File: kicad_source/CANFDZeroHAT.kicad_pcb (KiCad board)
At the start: 2 copper layers, 65 x 30 mm, 2 parts, among them CN1 RASPI-IO

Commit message: generated schematic and layout
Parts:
- removed ?: , 
- added C1: 100nF, capacitors:C_0603, F.Cu at (133.5, 96.5)
- added C2: 22pF, capacitors:C_0603, F.Cu at (141.0, 106.0)
- added C3: 22pF, capacitors:C_0603, F.Cu at (141.0, 100.0)
- added C4: 100nF, capacitors:C_0603, F.Cu at (154.5, 97.5)
- added CN2: CONN_01X04, CON_wuerth:WR-TBL_691210910004, F.Cu at (135.5, 113.0)
- added CN3: GH_SM04B-GHS-TB, Connector_JST:JST_GH_SM04B-GHS-TB_1x04-1MP_P1.25mm_Horizontal, F.Cu at (159.5, 113.0)
- added CN4: GH_SM04B-GHS-TB, Connector_JST:JST_GH_SM04B-GHS-TB_1x04-1MP_P1.25mm_Horizontal, F.Cu at (149.0, 113.0)
- added D1: DNI, diodes:SOD-123, F.Cu at (142.5, 108.5)
- added L1: Label, labels:generationmake_small_solder, F.Cu at (164.4, 98.5)
- added L2: Label, labels:generationmake_logo, F.Cu at (119.6, 100.7)
- added R1: 0R, resistors:R_0603, F.Cu at (148.5, 94.5)
- added R2: DNI, resistors:R_0603, F.Cu at (150.5, 94.5)
- added R3: 10k, resistors:R_0603, F.Cu at (152.5, 94.5)
- added R4: 120R, resistors:R_0603, F.Cu at (127.0, 103.5)
- added R5: 10k, resistors:R_0603, F.Cu at (137.0, 94.5)
- added SW1: JS202011JCQN, mechanical-switches:CK_JS202011JCQN, F.Cu at (122.7, 105.5)
- added U1: MCP2517FD, SOIC:SOIC-14_3.9x8.7mm_Pitch1.27mm, F.Cu at (148.0, 101.5)
- added U2: SN65HVD232, SOIC:SOIJ-8_5.3x5.3mm_Pitch1.27mm, F.Cu at (133.5, 102.5)
- added Y1: RH100-20.000-20-3030-TR, crystals:Crystal_SMD_3.2x2.5mm_4Pad, F.Cu at (141.0, 103.0)
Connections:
- CN1 pad 19: (no net) -> /SPI_MOSI
- CN1 pad 21: (no net) -> /SPI_MISO
- CN1 pad 22: (no net) -> /MCP2517_INT
- CN1 pad 23: (no net) -> /SPI_CLK
- CN1 pad 24: (no net) -> /SPI_CE0
- CN1 pad 26: (no net) -> /SPI_CE1
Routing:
- net GND: track 0.00 -> 156.8 mm, vias 0 -> 4
- net +3V3: track 0.00 -> 55.5 mm, vias 0 -> 2
- net /CANH: track 0.00 -> 52.9 mm
- net +5V: track 0.00 -> 48.7 mm
- net /CANL: track 0.00 -> 48.5 mm
- net /MCP2517_INT: track 0.00 -> 33.7 mm, vias 0 -> 1
- net /SPI_CLK: track 0.00 -> 27.2 mm
- net /CANVCC: track 0.00 -> 18.9 mm
- net /SPI_MOSI: track 0.00 -> 17.7 mm
- net /CAN_RX: track 0.00 -> 16.5 mm
- net /SPI_MISO: track 0.00 -> 14.7 mm
- net /CAN_TX: track 0.00 -> 12.4 mm
- net /MCP2517_CS: track 0.00 -> 9.68 mm
- net /SPI_CE0: track 0.00 -> 7.97 mm
- net /SPI_CE1: track 0.00 -> 7.90 mm
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- added copper zone on B.Cu, net GND
- added copper zone on F.Cu, net GND

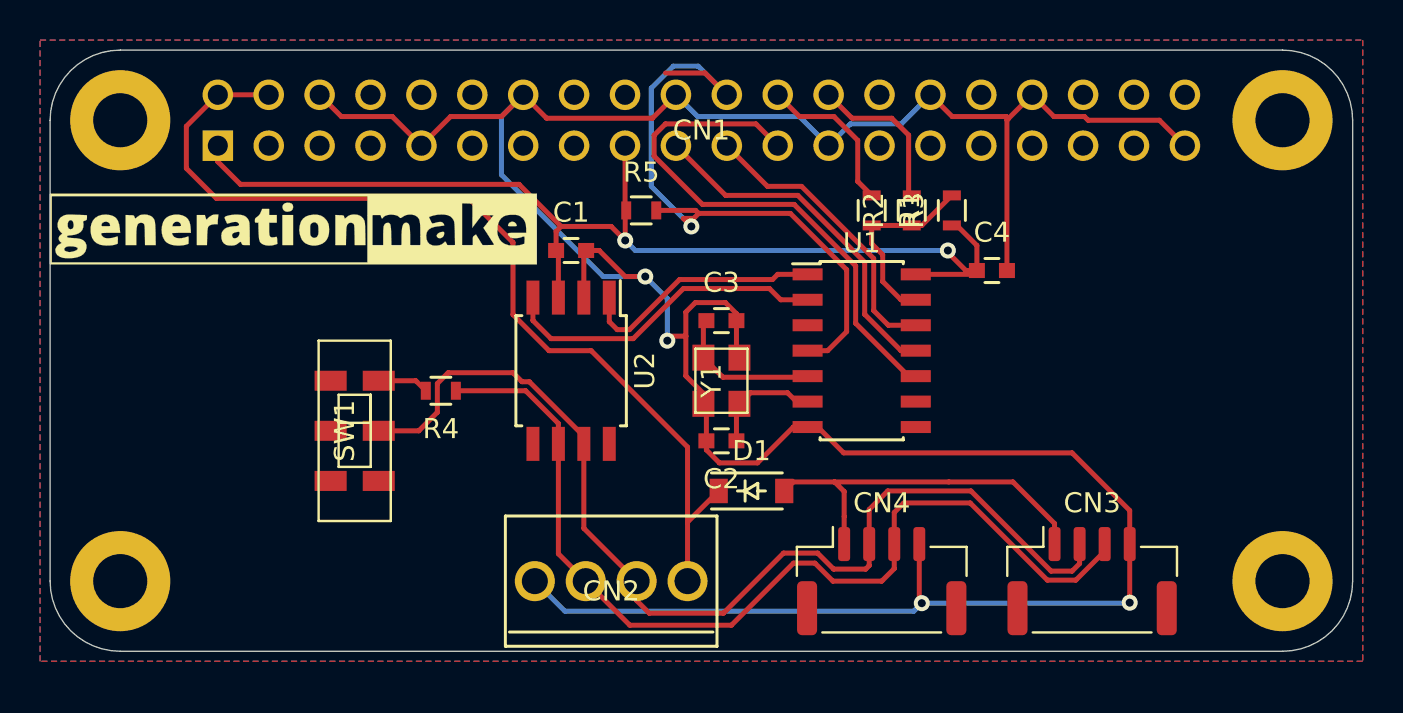
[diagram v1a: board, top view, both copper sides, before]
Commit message: added option resistors, updated layout
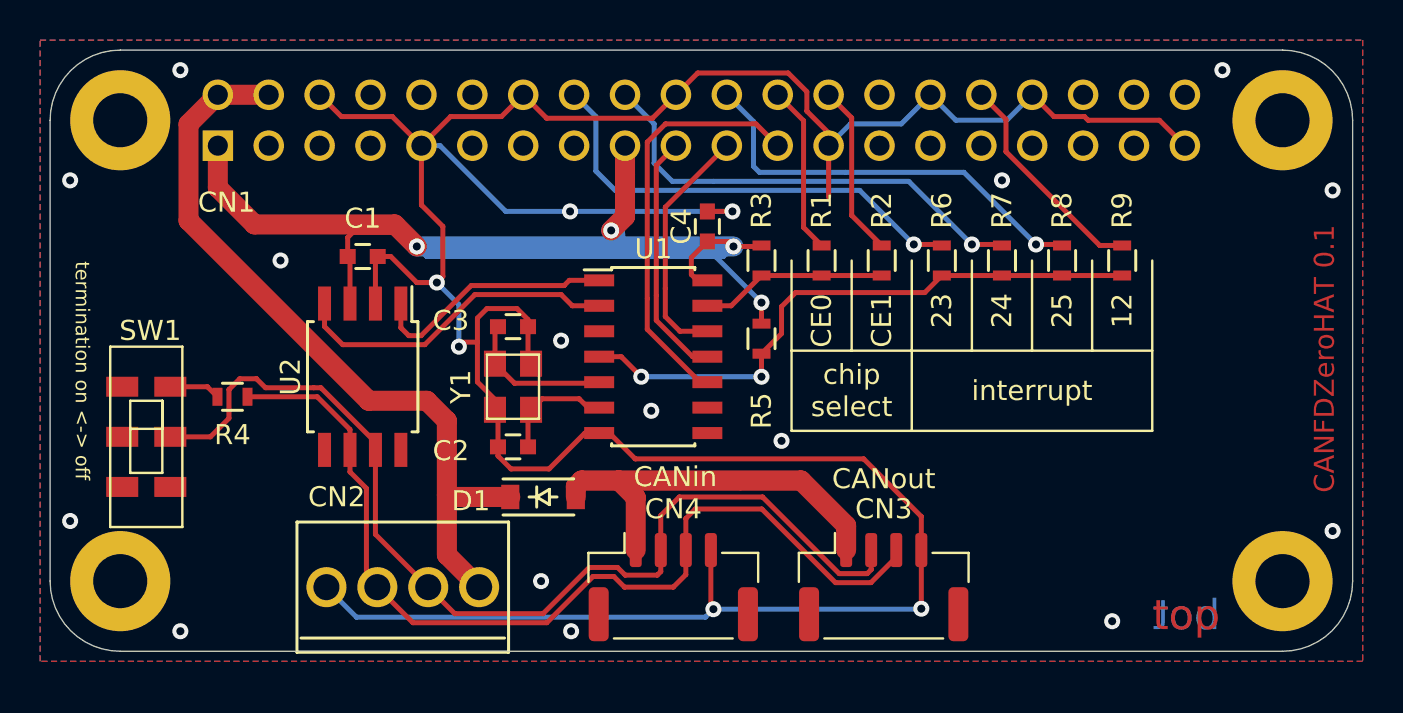
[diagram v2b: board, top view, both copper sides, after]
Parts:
- added R6: 0R, resistors:R_0603, F.Cu at (152.0, 97.0)
- added R7: 0R, resistors:R_0603, F.Cu at (155.0, 97.0)
- added R8: 0R, resistors:R_0603, F.Cu at (158.0, 97.0)
- added R9: 0R, resistors:R_0603, F.Cu at (161.0, 97.0)
- L2: moved to B.Cu
- moved L2 20.7 mm to (140.0, 104.0), turned to 180 degrees
- moved C4 14.4 mm to (140.3, 95.3), turned to 90 degrees
- moved C1 10.4 mm to (123.1, 96.8)
- moved C2 10.4 mm to (130.6, 106.3)
- moved C3 10.4 mm to (130.6, 100.3)
- moved CN2 10.4 mm to (125.1, 113.3)
- moved CN3 10.4 mm to (149.1, 113.3)
- moved CN4 10.4 mm to (138.6, 113.3)
- moved D1 10.4 mm to (132.1, 108.8)
- moved R4 10.4 mm to (116.6, 103.8)
- moved SW1 10.4 mm to (112.3, 105.8)
- moved U1 10.4 mm to (137.6, 101.8)
- moved U2 10.4 mm to (123.1, 102.8)
- moved Y1 10.4 mm to (130.6, 103.3)
- moved R3 9.82 mm to (143.0, 97.0), turned to 270 degrees
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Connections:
- CN1 pad 16: (no net) -> /INTERRUPT_23
- CN1 pad 18: (no net) -> /INTERRUPT_24
- CN1 pad 22: /MCP2517_INT -> /INTERRUPT_25
- CN1 pad 32: (no net) -> /INTERRUPT_12
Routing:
- net /INTERRUPT_24: track 0.00 -> 23.1 mm, vias 0 -> 1
- net /INTERRUPT_23: track 0.00 -> 23.1 mm, vias 0 -> 1
- net /INTERRUPT_25: track 0.00 -> 21.2 mm, vias 0 -> 1
- net /CANVCC: track 18.9 -> 39.0 mm
- net +3V3: track 55.5 -> 68.8 mm, vias 2 -> 4
- net /INTERRUPT_12: track 0.00 -> 11.1 mm
- net +5V: track 48.7 -> 38.6 mm
- net GND: track 156.8 -> 165.5 mm, vias 4 -> 21
- net /SPI_CLK: track 27.2 -> 20.8 mm
- net /SPI_MOSI: track 17.7 -> 12.4 mm
- net /MCP2517_INT: track 33.7 -> 30.1 mm, vias 1 -> 2
- net /SPI_MISO: track 14.7 -> 12.2 mm
- net /CANH: track 52.9 -> 51.6 mm
- net /CANL: track 48.5 -> 47.7 mm
- net /SPI_CE1: track 7.90 -> 8.62 mm
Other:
- board text added: "12"
- board text added: "23"
- board text added: "24"
- board text added: "25"
- board text added: "CANFDZeroHAT 0.1"
- board text added: "CANH"
- board text added: "CANL"
- board text added: "CANVCC"
- board text added: "CANin"
- board text added: "CANout"
- board text added: "CE0"
- board text added: "CE1"
- board text added: "GND"
- board text added: "VCC"
- board text added: "bot"
- board text added: "chip select"
- board text added: "for Microchip MCP2517FD or MCP2518FD"
- board text added: "interrupt"
- board text added: "termination on <-> off"
- board text added: "top"

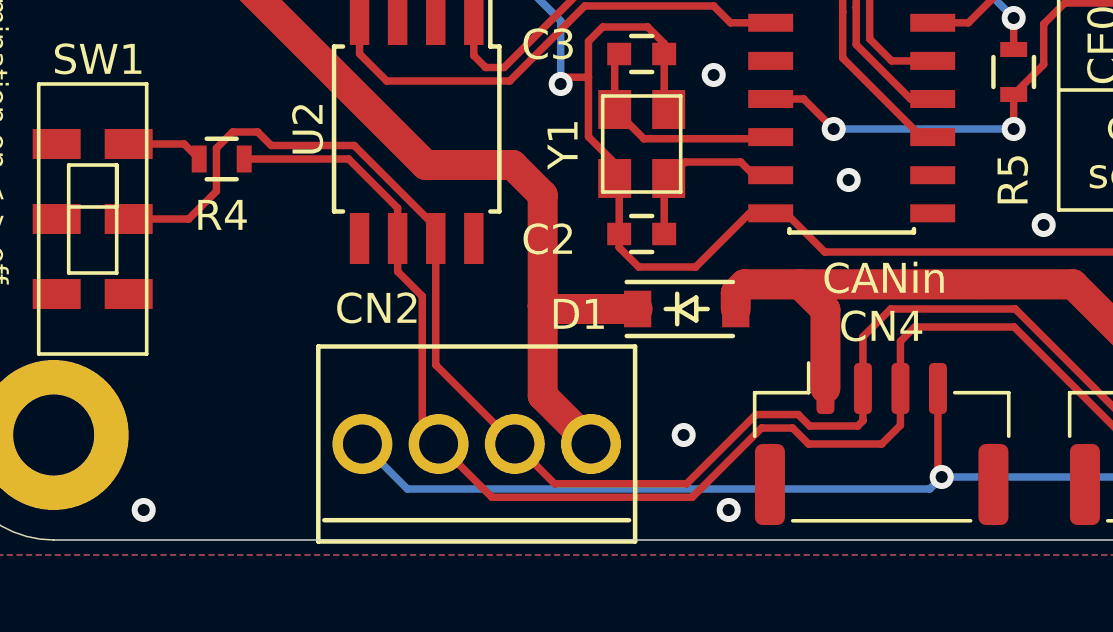
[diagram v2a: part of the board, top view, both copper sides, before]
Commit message: updated some part numbers
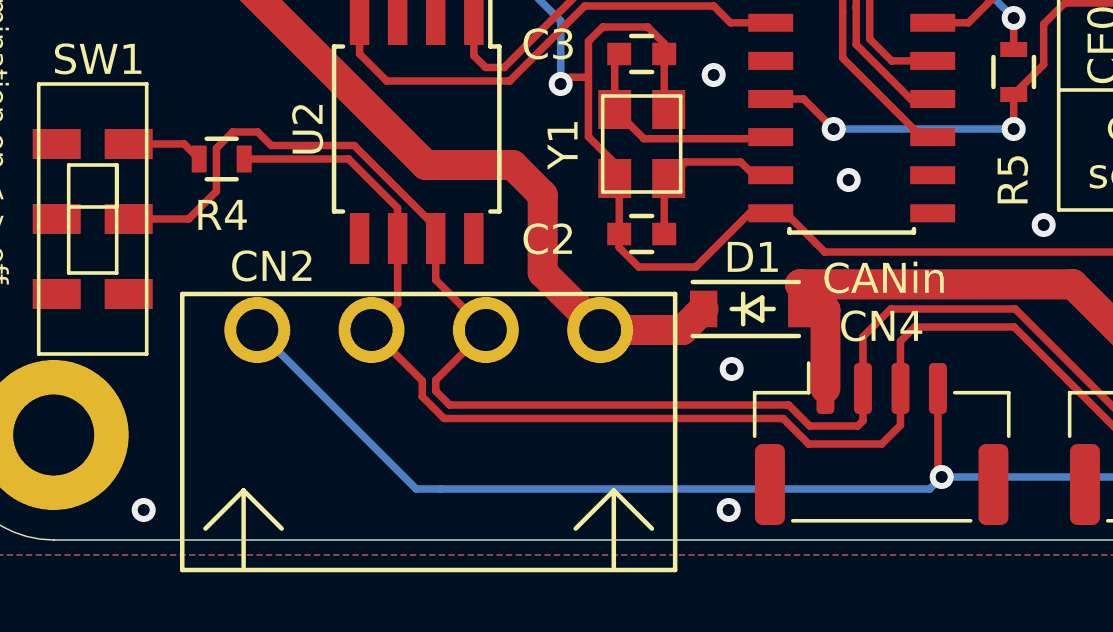
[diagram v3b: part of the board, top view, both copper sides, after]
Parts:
- CN2: value CONN_01X04 -> 691322310004; footprint CON_wuerth:WR-TBL_691210910004 -> CON_wuerth:WR-TBL_691322310004
- R6, R7, R9: value 0R -> DNI
- U1: value MCP2517FD -> MCP2518FD
- U2: value SN65HVD232 -> TCAN332GDR
- moved CN2 4.12 mm to (123.5, 109.5)
- moved D1 2.20 mm to (134.3, 108.8)
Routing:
- net /CANVCC: track 39.0 -> 33.5 mm
- net GND: track 165.5 -> 170.6 mm
- net +5V: track 38.6 -> 35.5 mm
- net /CANL: track 47.7 -> 45.9 mm
